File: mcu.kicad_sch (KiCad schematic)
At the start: 1 part, among them U1 ESP32-S3-WROOM-1

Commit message: almost done
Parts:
- added C3: 22u, Capacitor_SMD:C_0805_2012Metric_Pad1.18x1.45mm_HandSolder, symbol Device:C
- added C4, C8: 0.1u, Capacitor_SMD:C_0805_2012Metric_Pad1.18x1.45mm_HandSolder, symbol Device:C
- added C5: 1u, Capacitor_SMD:C_0805_2012Metric_Pad1.18x1.45mm_HandSolder, symbol Device:C
- added J1, J2, J5, J6: Conn_01x02_Pin, Connector_PinHeader_2.54mm:PinHeader_1x02_P2.54mm_Vertical, symbol Connector:Conn_01x02_Pin
- added J4: Conn_01x09_Pin, Connector_PinHeader_2.54mm:PinHeader_1x09_P2.54mm_Vertical, symbol Connector:Conn_01x09_Pin
- added R6, R8, R9: 10k, Resistor_SMD:R_0805_2012Metric_Pad1.20x1.40mm_HandSolder, symbol Device:R
- added SW85, SW86, SW87, SW89: SW_Push, Button_Switch_THT:SW_PUSH_6mm, symbol Switch:SW_Push
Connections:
- net GND: now reaches U1.1 (GND), U1.40 (GND), U1.41 (GND)
- net GND: now also C3.2, C4.2, C5.1, C8.1, J1.2 (Pin_2), J2.2 (Pin_2), J6.2 (Pin_2), R8.2, R9.2, SW85.1, SW86.2
- net col6: now reaches U1.10 (GPIO17/U1TXD/ADC2_CH6)
- net col7: now reaches U1.11 (GPIO18/U1RXD/ADC2_CH7/CLK_OUT3)
- net col8: now reaches U1.12 (GPIO8/TOUCH8/ADC1_CH7/SUBSPICS1)
- net USB_D-: now reaches U1.13 (GPIO19/U1RTS/ADC2_CH8/CLK_OUT2/USB_D-)
- net USB_D+: now reaches U1.14 (GPIO20/U1CTS/ADC2_CH9/CLK_OUT1/USB_D+)
- net col9: now reaches U1.15 (GPIO3/TOUCH3/ADC1_CH2)
- net col10: now reaches U1.16 (GPIO46)
- net col11: now reaches U1.17 (GPIO9/TOUCH9/ADC1_CH8/FSPIHD/SUBSPIHD)
- net col12: now reaches U1.18 (GPIO10/TOUCH10/ADC1_CH9/FSPICS0/FSPIIO4/SUBSPICS0)
- net col13: now reaches U1.19 (GPIO11/TOUCH11/ADC2_CH0/FSPID/FSPIIO5/SUBSPID)
- net +3.3V: now reaches U1.2 (3V3)
- net +3.3V: now also C3.1, C4.1, J6.1 (Pin_1), R6.1, SW87.1, SW89.1
- net row0: now reaches U1.20 (GPIO12/TOUCH12/ADC2_CH1/FSPICLK/FSPIIO6/SUBSPICLK)
- net row1: now reaches U1.21 (GPIO13/TOUCH13/ADC2_CH2/FSPIQ/FSPIIO7/SUBSPIQ)
- net row2: now reaches U1.22 (GPIO14/TOUCH14/ADC2_CH3/FSPIWP/FSPIDQS/SUBSPIWP)
- net row3: now reaches U1.23 (GPIO21)
- net at U1.24 (GPIO47/SPICLK_P/SUBSPICLK_P_DIFF): now also J4.9 (Pin_9)
- net at U1.25 (GPIO48/SPICLK_N/SUBSPICLK_N_DIFF): now also J4.8 (Pin_8)
- net row4: now reaches U1.26 (GPIO45)
- net BOOT: now reaches U1.27 (GPIO0/BOOT)
- net BOOT: now also J2.1 (Pin_1), SW86.1
- net at U1.28 (SPIIO6/GPIO35/FSPID/SUBSPID): now also J4.5 (Pin_5)
- net at U1.29 (SPIIO7/GPIO36/FSPICLK/SUBSPICLK): now also J4.6 (Pin_6)
- net at U1.3 (EN): now also C5.2, C8.2, J1.1 (Pin_1), R6.2, SW85.2
- net at U1.30 (SPIDQS/GPIO37/FSPIQ/SUBSPIQ): now also J4.7 (Pin_7)
- net row5: now reaches U1.31 (GPIO38/FSPIWP/SUBSPIWP)
- net at U1.32 (MTCK/GPIO39/CLK_OUT3/SUBSPICS1): now also J4.1 (Pin_1), R8.1, SW89.2
- net at U1.33 (MTDO/GPIO40/CLK_OUT2): now also J4.2 (Pin_2), R9.1, SW87.2
- net at U1.34 (MTDI/GPIO41/CLK_OUT1): now also J4.3 (Pin_3)
- net at U1.35 (MTMS/GPIO42): now also J4.4 (Pin_4)
- net at U1.38 (GPIO2/TOUCH2/ADC1_CH1): now also J5.1 (Pin_1)
- net at U1.39 (GPIO1/TOUCH1/ADC1_CH0): now also J5.2 (Pin_2)
- net col0: now reaches U1.4 (GPIO4/TOUCH4/ADC1_CH3)
- net col1: now reaches U1.5 (GPIO5/TOUCH5/ADC1_CH4)
- net col2: now reaches U1.6 (GPIO6/TOUCH6/ADC1_CH5)
- net col3: now reaches U1.7 (GPIO7/TOUCH7/ADC1_CH6)
- net col4: now reaches U1.8 (GPIO15/U0RTS/ADC2_CH4/XTAL_32K_P)
- net col5: now reaches U1.9 (GPIO16/U0CTS/ADC2_CH5/XTAL_32K_N)
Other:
- moved on the sheet: U1

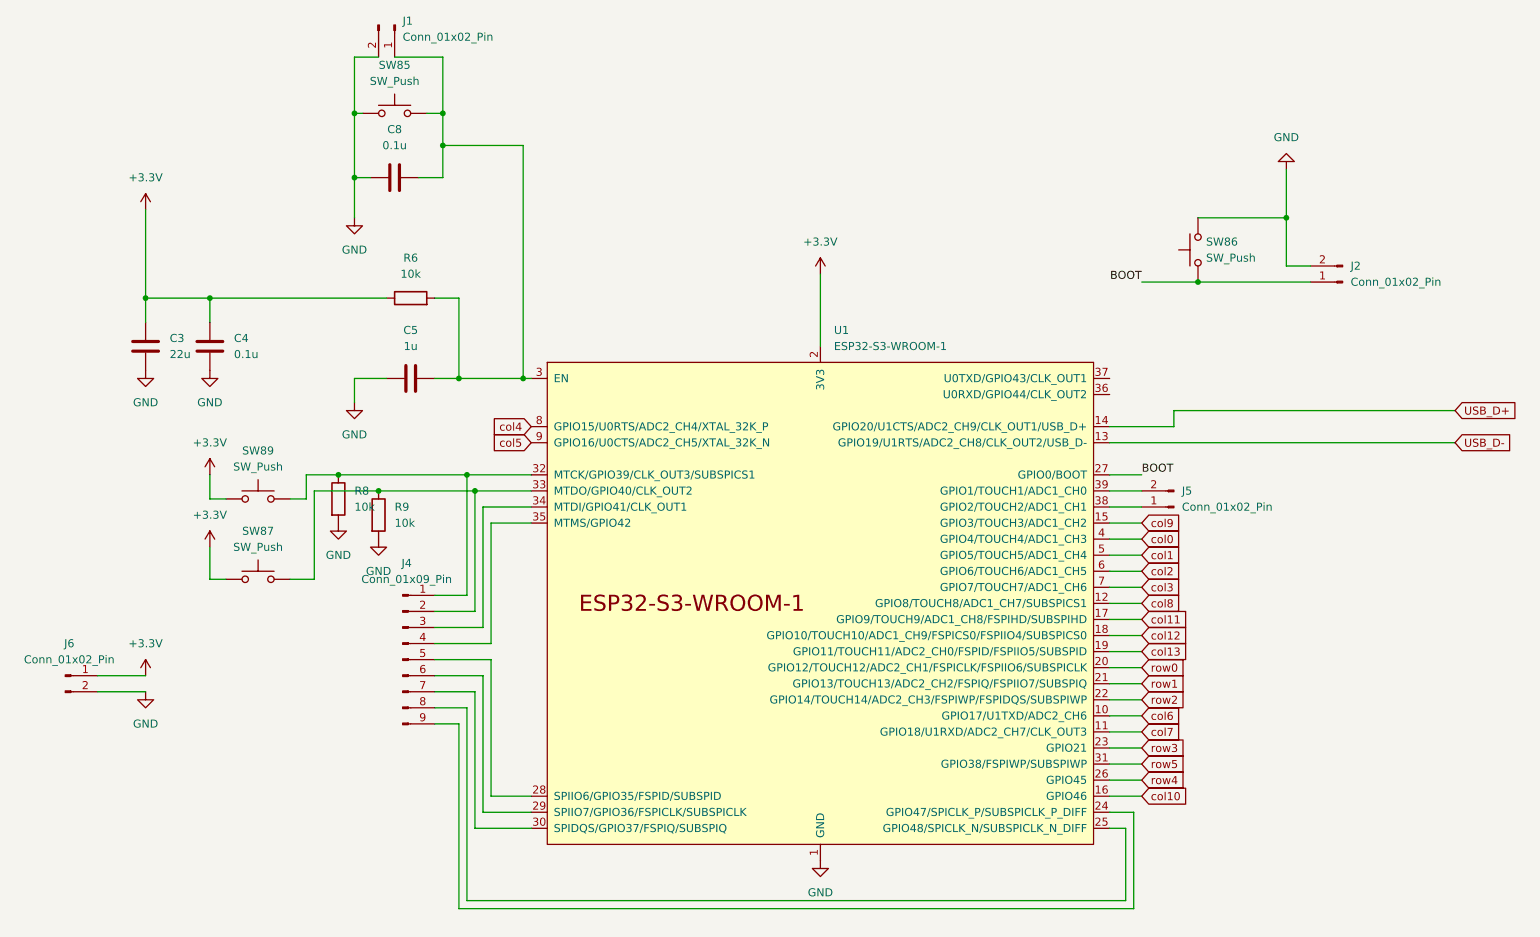
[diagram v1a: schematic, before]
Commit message: added more leds pins, fixed rule errors.
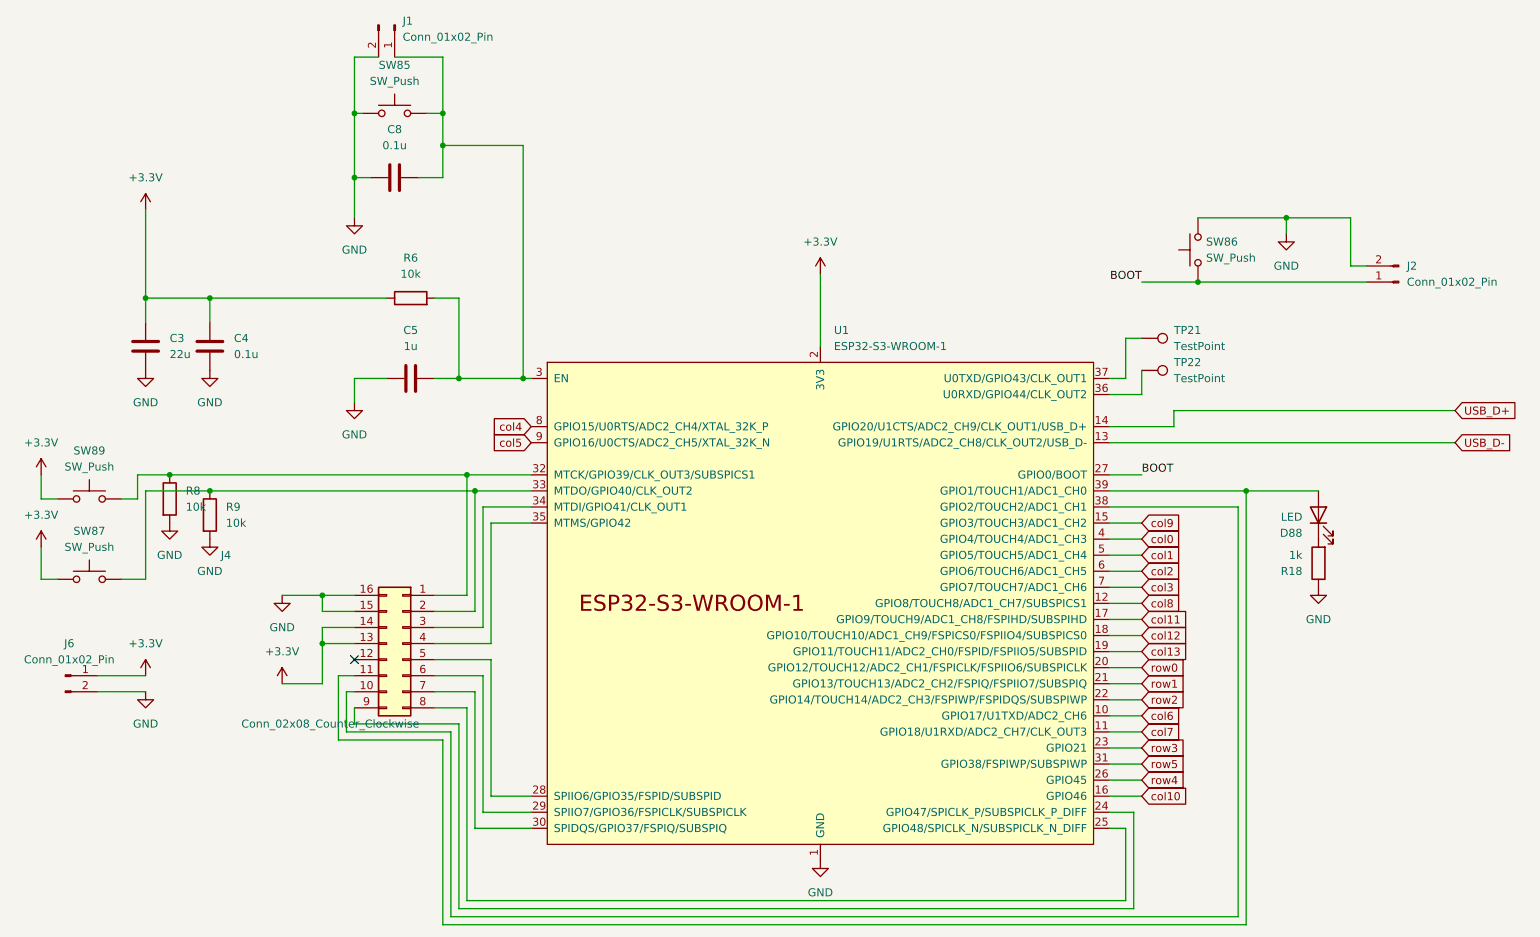
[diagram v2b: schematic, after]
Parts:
- removed J4: Conn_01x09_Pin, Connector_PinHeader_2.54mm:PinHeader_1x09_P2.54mm_Vertical, symbol Connector:Conn_01x09_Pin
- removed J5: Conn_01x02_Pin, Connector_PinHeader_2.54mm:PinHeader_1x02_P2.54mm_Vertical, symbol Connector:Conn_01x02_Pin
- added D88: LED, LED_SMD:LED_0805_2012Metric_Pad1.15x1.40mm_HandSolder, symbol Device:LED
- added J4: Conn_02x08_Counter_Clockwise, Connector_PinHeader_2.54mm:PinHeader_2x08_P2.54mm_Vertical, symbol Connector_Generic:Conn_02x08_Counter_Clockwise
- added R18: 1k, Resistor_SMD:R_0805_2012Metric_Pad1.20x1.40mm_HandSolder, symbol Device:R
- added TP21, TP22: TestPoint, TestPoint:TestPoint_Pad_D1.0mm, symbol Connector:TestPoint
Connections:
- net +3.3V: now also J4.13 (Pin_13), J4.14 (Pin_14)
- net GND: now also J4.15 (Pin_15), J4.16 (Pin_16), R18.1
- net at R8.1, SW89.2, U1.32 (MTCK/GPIO39/CLK_OUT3/SUBSPICS1): now also J4.1 (Pin_1)
- net at U1.38 (GPIO2/TOUCH2/ADC1_CH1): now also J4.10 (Pin_10)
- net at U1.39 (GPIO1/TOUCH1/ADC1_CH0): now also D88.2 (A), J4.11 (Pin_11)
- net at U1.24 (GPIO47/SPICLK_P/SUBSPICLK_P_DIFF): now also J4.9 (Pin_9)
- net at U1.25 (GPIO48/SPICLK_N/SUBSPICLK_N_DIFF): now also J4.8 (Pin_8)
- net at U1.28 (SPIIO6/GPIO35/FSPID/SUBSPID): now also J4.5 (Pin_5)
- net at U1.29 (SPIIO7/GPIO36/FSPICLK/SUBSPICLK): now also J4.6 (Pin_6)
- net at U1.30 (SPIDQS/GPIO37/FSPIQ/SUBSPIQ): now also J4.7 (Pin_7)
- net at R9.1, SW87.2, U1.33 (MTDO/GPIO40/CLK_OUT2): now also J4.2 (Pin_2)
- net at U1.34 (MTDI/GPIO41/CLK_OUT1): now also J4.3 (Pin_3)
- net at U1.35 (MTMS/GPIO42): now also J4.4 (Pin_4)
- net at U1.36 (U0RXD/GPIO44/CLK_OUT2): now also TP22.1
- net at U1.37 (U0TXD/GPIO43/CLK_OUT1): now also TP21.1
- new net: D88.1 (K), R18.2
- no-connect marks 0 -> 1
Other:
- moved on the sheet: J2, R8, R9, SW87, SW89

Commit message: sent to fab
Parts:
- removed C8: 0.1u, Capacitor_SMD:C_0805_2012Metric_Pad1.18x1.45mm_HandSolder, symbol Device:C
- removed J1, J2: Conn_01x02_Pin, Connector_PinHeader_2.54mm:PinHeader_1x02_P2.54mm_Vertical, symbol Connector:Conn_01x02_Pin
- added R19: 10k, Resistor_SMD:R_0805_2012Metric_Pad1.20x1.40mm_HandSolder, symbol Device:R
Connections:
- net +3.3V: now also R6.2, R19.2; no longer R6.1
- net BOOT: now also R19.1
- net at C5.2, SW85.2, U1.3 (EN): now also R6.1; no longer R6.2
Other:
- moved on the sheet: C5, R6, SW85, SW86
